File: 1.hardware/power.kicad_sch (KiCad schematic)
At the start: 74 parts, among them IC8 LMR51610XDBVR, J4 12V~48V BAT, J5 12V-48V Jack, SW1 SW_DPST_x2

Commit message: 중간 저장
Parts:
- removed SW1: SW_DPST_x2, symbol Switch:SW_DPST_x2
- added SW1: SW_Push, symbol Switch:SW_Push
- C2: renamed from C62; footprint (none) -> Capacitor_SMD:C_Elec_6.3x5.4
- C26: renamed from C27; footprint Capacitor_SMD:C_0402_1005Metric -> Capacitor_SMD:C_0603_1608Metric
- C27: renamed from C35; footprint Capacitor_SMD:C_0402_1005Metric -> Capacitor_SMD:C_0603_1608Metric
- C28: renamed from C66; footprint Capacitor_SMD:C_0402_1005Metric -> Capacitor_SMD:C_0603_1608Metric
- C5: renamed from C73; footprint (none) -> Capacitor_SMD:C_Elec_5x5.8
- C6: renamed from C74; footprint (none) -> Capacitor_SMD:C_Elec_5x5.8
- C8: renamed from C75; footprint (none) -> Capacitor_SMD:C_Elec_4x5.4
- H1, H2, H3, H4: footprint (none) -> MountingHole:MountingHole_3.2mm_M3
- R1: renamed from R145; footprint (none) -> Resistor_SMD:R_0603_1608Metric
- R10: renamed from R8; footprint (none) -> Resistor_SMD:R_0603_1608Metric
- R11: renamed from R147; footprint (none) -> Resistor_SMD:R_0603_1608Metric
- R12: renamed from R148; footprint (none) -> Resistor_SMD:R_0603_1608Metric
- R13: renamed from R150; footprint (none) -> Resistor_SMD:R_0603_1608Metric
- R14: renamed from R151; footprint (none) -> Resistor_SMD:R_0603_1608Metric
- R2: renamed from R146; footprint (none) -> Resistor_SMD:R_0603_1608Metric
- R3: renamed from R4; footprint (none) -> Resistor_SMD:R_0603_1608Metric
- R4: renamed from R5; footprint (none) -> Resistor_SMD:R_0603_1608Metric
- R5: renamed from R6; footprint (none) -> Resistor_SMD:R_0402_1005Metric
- R6: renamed from R7; footprint (none) -> Resistor_SMD:R_0402_1005Metric
- R7: renamed from R149; footprint (none) -> Resistor_SMD:R_0402_1005Metric
- R8: renamed from R152; footprint (none) -> Resistor_SMD:R_0402_1005Metric
- R9: footprint (none) -> Resistor_SMD:R_0603_1608Metric
- TP1, TP3, TP5: footprint (none) -> TestPoint:TestPoint_Pad_D1.5mm
- TP2: value TestPoint -> TP_Ext_Volt; footprint (none) -> TestPoint:TestPoint_Pad_D1.5mm
- TP4: renamed from TP6; footprint (none) -> TestPoint:TestPoint_Pad_D1.5mm
- TP6: renamed from TP4; footprint (none) -> TestPoint:TestPoint_Pad_D1.5mm
- renumbered C56 to C1, C26 to C10, C29 to C11, C31 to C12, C33 to C13, C36 to C14, C64 to C15, C72 to C16, C28 to C17, C30 to C18, C34 to C19, C37 to C20, C65 to C21, C76 to C22, C32 to C23, C63 to C24, C77 to C25, C22 to C3, C23 to C4, C24 to C7, C25 to C9, D6 to D1, D13 to D3, D1 to D4, D3 to D5, D4 to D6, D5 to D7, IC8 to IC1, J4 to J1, J5 to J2, L2 to L1, L4 to L2, L1 to L3, L3 to L4, L9 to L5, L5 to L6, L6 to L7, L10 to L8, PS5 to PS1, PS3 to PS2, PS4 to PS3
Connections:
- net at C4.1, D3.1, L2.1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: now also SW1.2
- net at D1.1 (K), D2.1 (K), TP1.1: now also SW1.1

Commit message: 중간 저장
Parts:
- D3: footprint DIONM5436X244N -> SamacSys_Parts:DIONM5436X244N
- D4, D5, D6, D7: footprint SOD2613X100N -> SamacSys_Parts:SOD2613X100N
- J1: value 12V~48V BAT -> 12V~48V BAT_XT60_MALE; footprint (none) -> Connector_AMASS:AMASS_XT60PW-M_1x02_P7.20mm_Horizontal
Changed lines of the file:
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@@
 			)
 		)
-		(property "Footprint" "SOD2613X100N"
+		(property "Footprint" "SamacSys_Parts:SOD2613X100N"
 			(at 109.22 55.88 0)
 			(effects
@@
 			)
 		)
-		(property "Footprint" "SOD2613X100N"
+		(property "Footprint" "SamacSys_Parts:SOD2613X100N"
 			(at 204.47 88.9 0)
 			(effects
@@
 			)
 		)
-		(property "Footprint" "SOD2613X100N"
+		(property "Footprint" "SamacSys_Parts:SOD2613X100N"
 			(at 203.2 44.45 0)
 			(effects
@@
 			)
 		)
-		(property "Footprint" "DIONM5436X244N"
+		(property "Footprint" "SamacSys_Parts:DIONM5436X244N"
 			(at 82.55 46.99 0)
 			(effects
@@
 			)
 		)
-		(property "Footprint" "SOD2613X100N"
+		(property "Footprint" "SamacSys_Parts:SOD2613X100N"
 			(at 204.47 133.35 0)
 			(effects
@@
 			)
 		)
-		(property "Value" "12V~48V BAT"
+		(property "Value" "12V~48V BAT_XT60_MALE"
 			(at 25.4 58.42 0)
 			(effects
@@
 			)
 		)
-		(property "Footprint" ""
+		(property "Footprint" "Connector_AMASS:AMASS_XT60PW-M_1x02_P7.20mm_Horizontal"
 			(at 25.4 52.07 0)
 			(effects

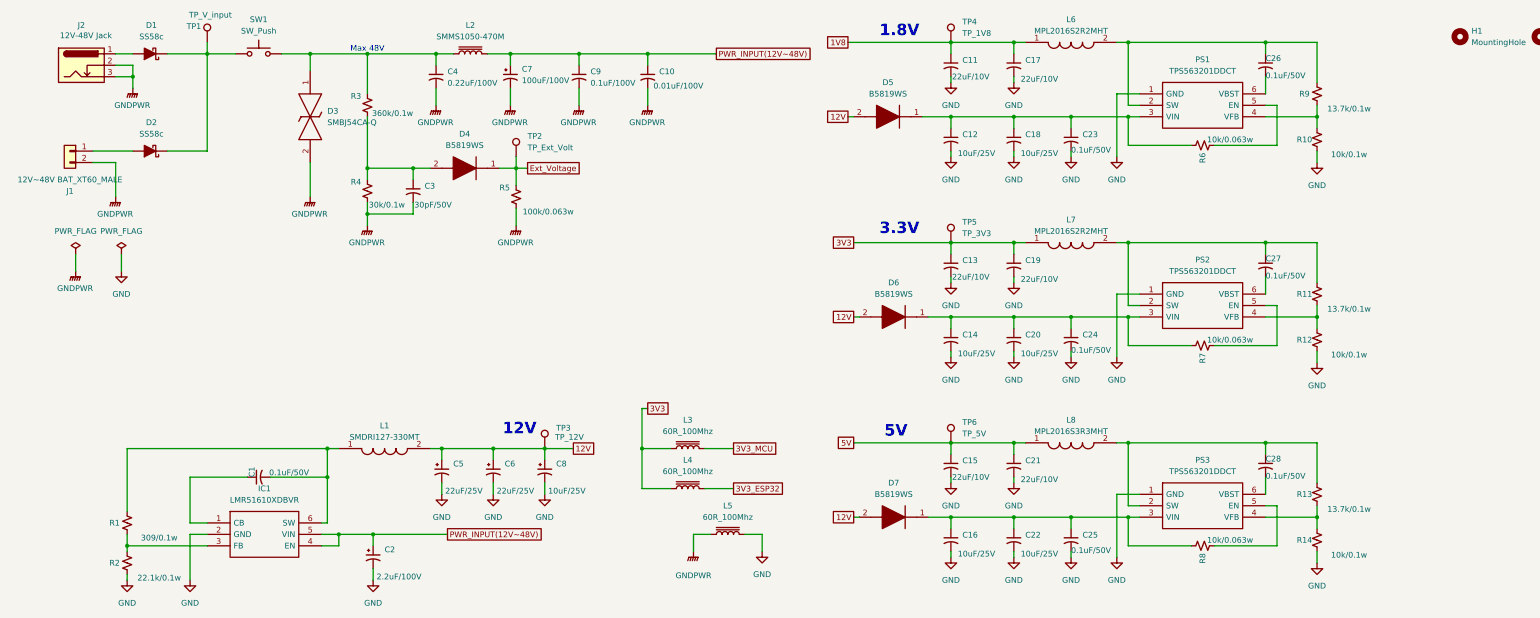
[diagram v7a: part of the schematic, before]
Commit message: 풋프린트 연결 완료
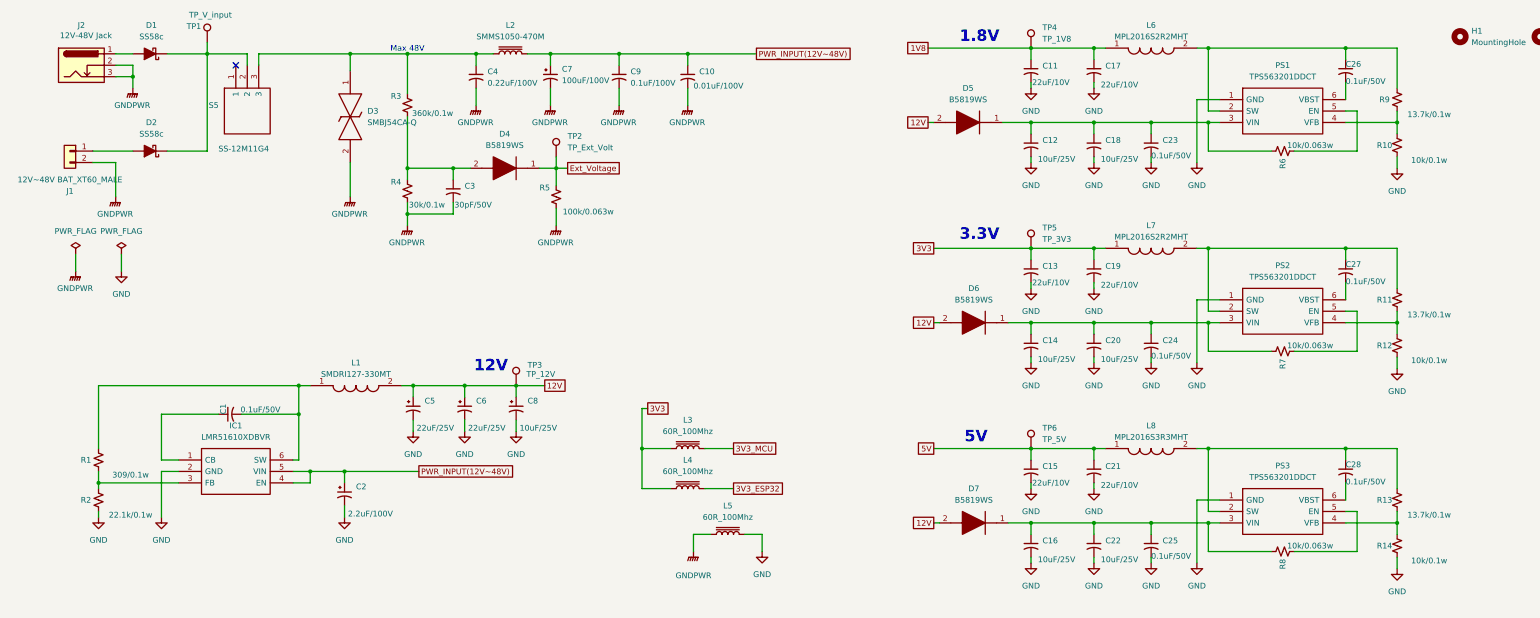
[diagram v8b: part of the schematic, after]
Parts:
- removed SW1: SW_Push, symbol Switch:SW_Push
- added S5: SS-12M11G4, SamacSys_Parts_Project:SS12M11G4, symbol SamacSys_Parts:SS-12M11G4
- D3: footprint SamacSys_Parts:DIONM5436X244N -> SamacSys_Parts_Project:DIOM5436X244N
- D4, D5, D6, D7: footprint SamacSys_Parts:SOD2613X100N -> SamacSys_Parts_Project:SOD2613X100N
- IC1: footprint SOT95P280X145-6N -> SamacSys_Parts_Project:SOT95P280X145-6N
- L1: footprint SMDRI127330MT -> SamacSys_Parts_Project:SMDRI127330MT
- L6, L7, L8: footprint SamacSys_Parts:INDC2116X100N -> SamacSys_Parts_Project:INDC2116X100N
- PS1, PS2, PS3: footprint SamacSys_Parts:SOT95P280X110-6N -> SamacSys_Parts_Project:SOT95P280X110-6N
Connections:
- net at C4.1, D3.1, L2.1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: now also S5.3
- net at D1.1 (K), D2.1 (K), TP1.1: now also S5.2
- no-connect marks 0 -> 1
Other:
- moved on the sheet: C1, C10, C11, C12, C13, C14, C15, C16, C17, C18, C19, C2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
